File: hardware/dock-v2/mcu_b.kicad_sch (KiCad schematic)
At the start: 31 parts, among them SW401 SW_Push, U401 RP2354A, Y401 12MHz

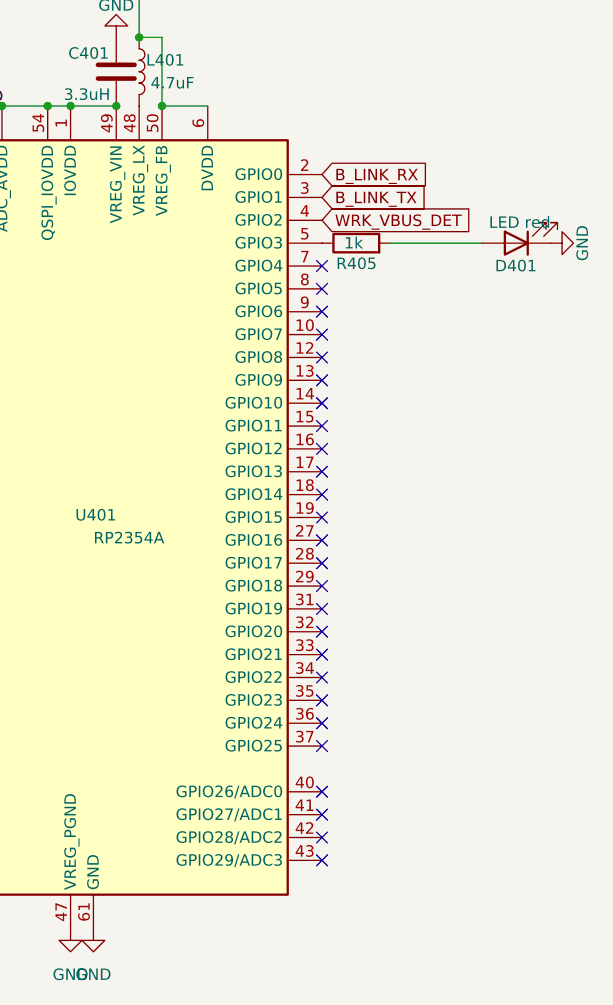
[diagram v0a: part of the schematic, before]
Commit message: Dock v2: MCU A/B GPIO map reassigned for routing (ESP32 front-left, 2-layer goal)
A: KBD PIO-USB on GPIO2/3 (DMDP), BLE on UART0 GPIO12/13, pogo on the
bottom pins, CH224A on I2C1 GPIO18/19 (+PG 17) routed under B, B
RUN/SWD on GPIO20-22, B link on UART1 GPIO23/24, BOOTSEL B on GPIO25,
ADC order reversed. B: link on GPIO5/6, WRK_VBUS_DET on GPIO29.
Docs: GPIO numbers in DOCK_CONNECTIONS now come from dock_nets.py.

Co-Authored-By: Claude Opus 5.5 <noreply@anthropic.com>
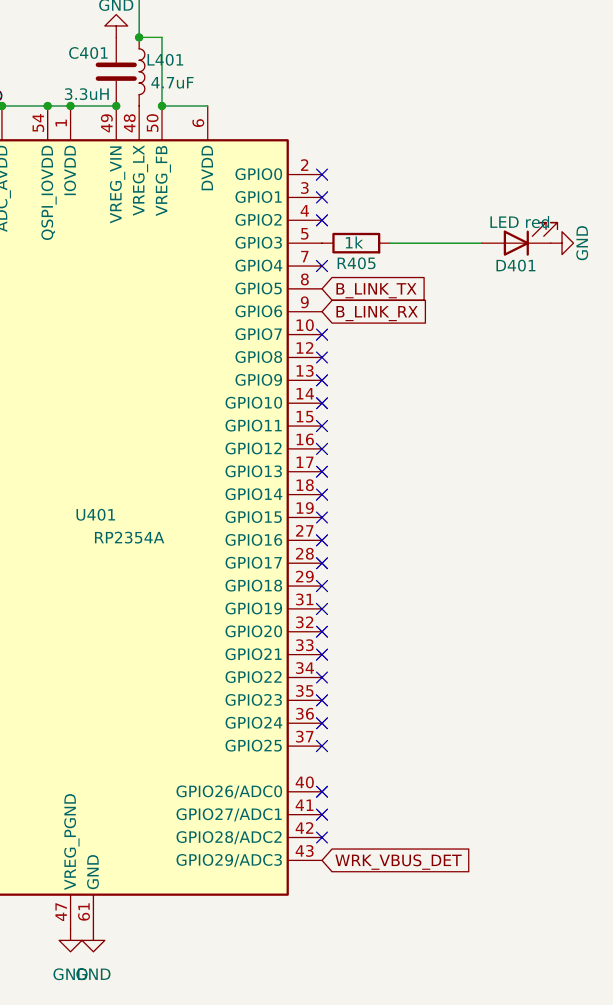
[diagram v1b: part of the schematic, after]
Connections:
- net B_LINK_RX: now also U401.9 (GPIO6); no longer U401.2 (GPIO0)
- net B_LINK_TX: now also U401.8 (GPIO5); no longer U401.3 (GPIO1)
- net WRK_VBUS_DET: now also U401.43 (GPIO29/ADC3); no longer U401.4 (GPIO2)
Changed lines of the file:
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@@
+	)
+	(no_connect
+		(at 182.88 137.16)
+	)
+	(no_connect
+		(at 182.88 139.7)
+	)
+	(no_connect
+		(at 182.88 142.24)
+	)
+	(no_connect
+		(at 182.88 147.32)
+	)
+	(no_connect
+		(at 182.88 154.94)
+	)
+	(no_connect
+		(at 132.08 172.72)
+	)
+	(no_connect
+		(at 132.08 180.34)
+	)
+	(no_connect
+		(at 182.88 157.48)
+	)
+	(no_connect
+		(at 182.88 160.02)
+	)
+	(no_connect
+		(at 182.88 162.56)
+	)
+	(no_connect
+		(at 182.88 165.1)
+	)
+	(no_connect
+		(at 182.88 167.64)
+	)
+	(no_connect
+		(at 132.08 182.88)
+	)
+	(no_connect
+		(at 182.88 170.18)
+	)
+	(no_connect
+		(at 182.88 172.72)
+	)
+	(no_connect
+		(at 182.88 175.26)
+	)
+	(no_connect
+		(at 132.08 175.26)
+	)
+	(no_connect
+		(at 182.88 177.8)
+	)
+	(no_connect
+		(at 182.88 180.34)
+	)
+	(no_connect
+		(at 182.88 182.88)
+	)
+	(no_connect
+		(at 182.88 185.42)
+	)
+	(no_connect
+		(at 182.88 187.96)
+	)
+	(no_connect
+		(at 182.88 190.5)
+	)
+	(no_connect
+		(at 182.88 193.04)
+	)
+	(no_connect
+		(at 132.08 177.8)
+	)
+	(no_connect
+		(at 182.88 195.58)
+	)
+	(no_connect
+		(at 182.88 198.12)
+	)
+	(no_connect
+		(at 182.88 200.66)
+	)
+	(no_connect
+		(at 182.88 205.74)
+	)
+	(no_connect
+		(at 182.88 208.28)
 	)
 	(no_connect
 		(at 182.88 210.82)
-	)
-	(no_connect
-		(at 182.88 177.8)
-	)
-	(no_connect
-		(at 182.88 167.64)
-	)
-	(no_connect
-		(at 182.88 213.36)
-	)
-	(no_connect
-		(at 182.88 200.66)
-	)
-	(no_connect
-		(at 132.08 172.72)
-	)
-	(no_connect
-		(at 132.08 180.34)
-	)
-	(no_connect
-		(at 182.88 175.26)
-	)
-	(no_connect
-		(at 182.88 162.56)
-	)
-	(no_connect
-		(at 182.88 187.96)
-	)
-	(no_connect
-		(at 182.88 180.34)
-	)
-	(no_connect
-		(at 182.88 149.86)
-	)
-	(no_connect
-		(at 132.08 182.88)
-	)
-	(no_connect
-		(at 182.88 147.32)
-	)
-	(no_connect
-		(at 182.88 198.12)
-	)
-	(no_connect
-		(at 182.88 205.74)
-	)
-	(no_connect
-		(at 132.08 175.26)
-	)
-	(no_connect
-		(at 182.88 157.48)
-	)
-	(no_connect
-		(at 182.88 160.02)
-	)
-	(no_connect
-		(at 182.88 195.58)
-	)
-	(no_connect
-		(at 182.88 152.4)
-	)
-	(no_connect
-		(at 182.88 182.88)
-	)
-	(no_connect
-		(at 182.88 190.5)
-	)
-	(no_connect
-		(at 182.88 172.72)
-	)
-	(no_connect
-		(at 132.08 177.8)
-	)
-	(no_connect
-		(at 182.88 185.42)
-	)
-	(no_connect
-		(at 182.88 170.18)
-	)
-	(no_connect
-		(at 182.88 165.1)
-	)
-	(no_connect
-		(at 182.88 208.28)
-	)
-	(no_connect
-		(at 182.88 154.94)
-	)
-	(no_connect
-		(at 182.88 193.04)
 	)
 	(wire
@@
 	(global_label "WRK_VBUS_DET"
 		(shape input)
-		(at 182.88 142.24 0)
+		(at 182.88 213.36 0)
 		(fields_autoplaced yes)
 		(effects
@@
 		)
 		(property "Intersheetrefs" "${INTERSHEET_REFS}"
-			(at 200.077 142.24 0)
+			(at 200.077 213.36 0)
 			(hide yes)
 			(show_name no)
@@
 	(global_label "B_LINK_RX"
 		(shape input)
-		(at 182.88 137.16 0)
+		(at 182.88 152.4 0)
 		(fields_autoplaced yes)
 		(effects
@@
 		)
 		(property "Intersheetrefs" "${INTERSHEET_REFS}"
-			(at 195.7833 137.16 0)
+			(at 195.7833 152.4 0)
 			(hide yes)
 			(show_name no)
@@
 	(global_label "B_LINK_TX"
 		(shape input)
-		(at 182.88 139.7 0)
+		(at 182.88 149.86 0)
 		(fields_autoplaced yes)
 		(effects
@@
 		)
 		(property "Intersheetrefs" "${INTERSHEET_REFS}"
-			(at 195.4809 139.7 0)
-			(hide yes)
-			(show_name no)
+			(at 195.4809 149.86 0)
+			(hide yes)
+			(show_name no)
